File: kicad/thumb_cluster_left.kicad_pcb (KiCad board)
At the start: 2 copper layers, 41.2 x 46.6 mm, 18 parts, among them J1 Conn_01x07

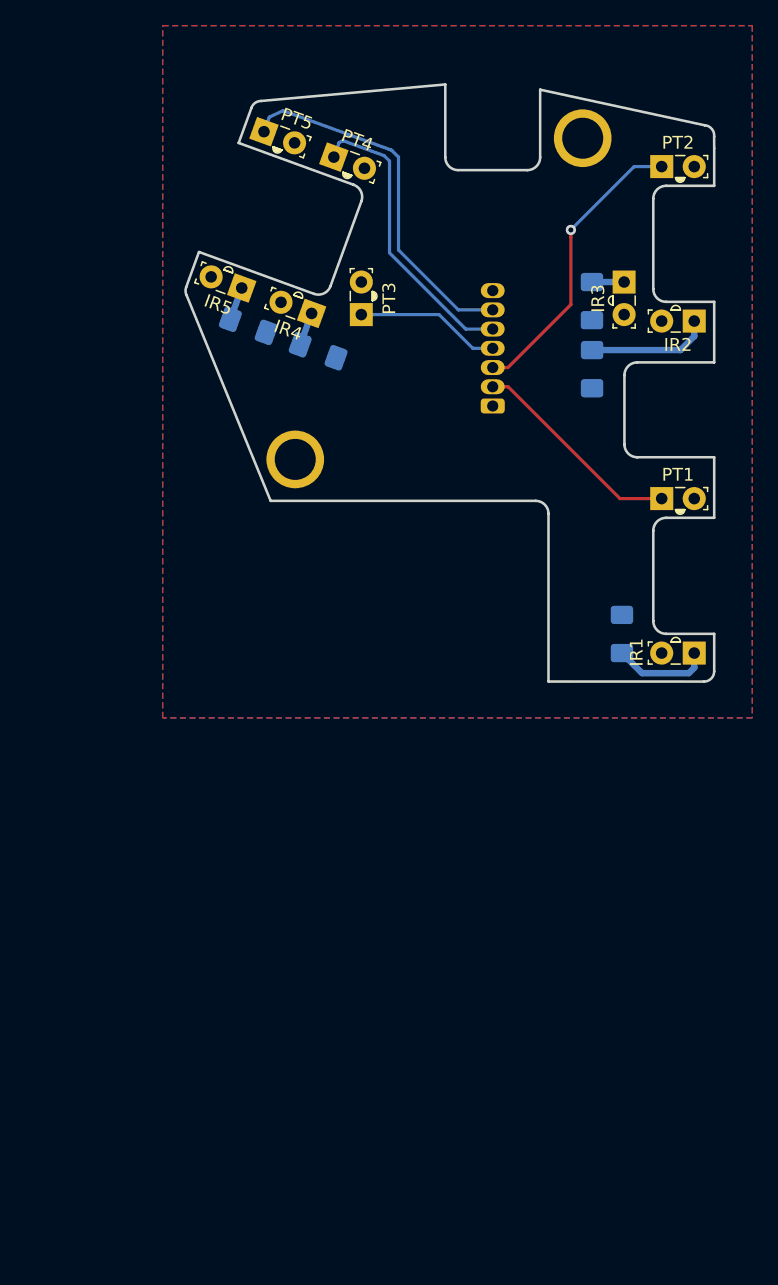
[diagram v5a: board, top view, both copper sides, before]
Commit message: Update thumb clusters to v2.5
Mostly just switching from 1206 to 0805 resistors, and some minor cleanup
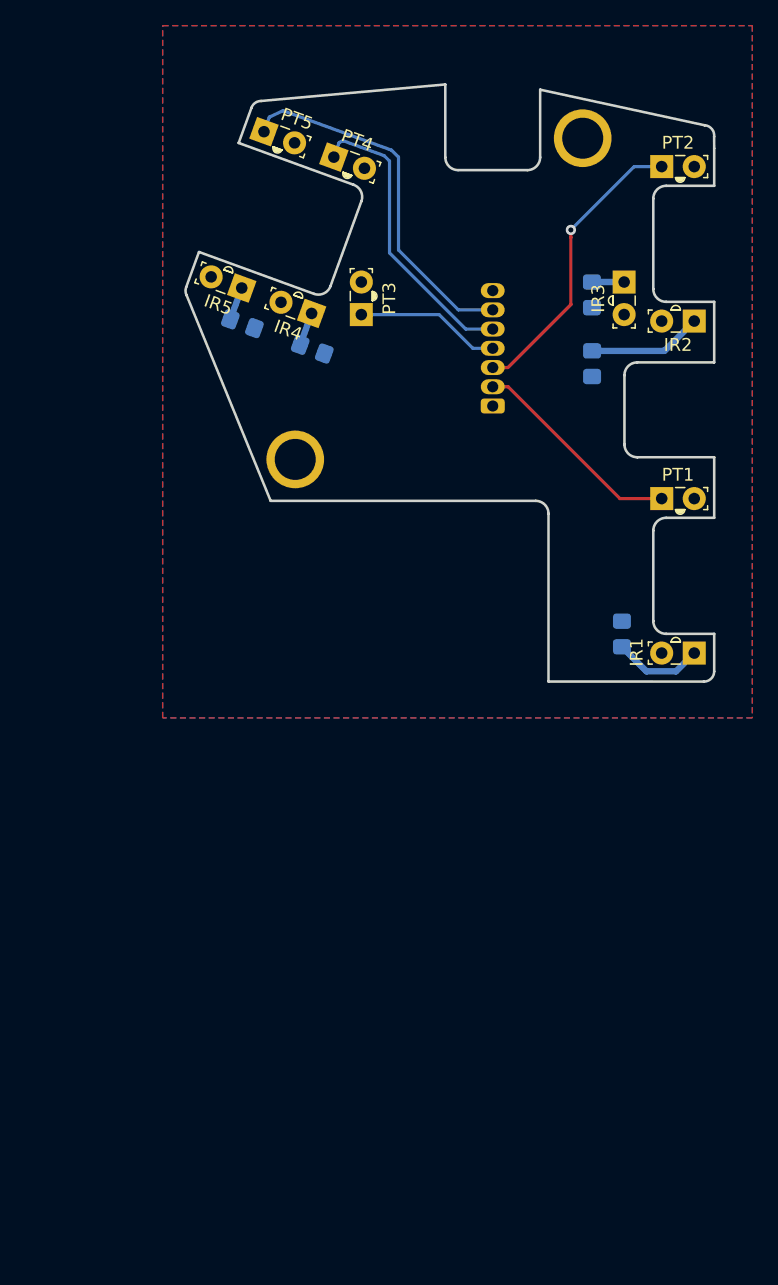
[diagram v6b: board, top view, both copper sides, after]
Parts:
- R1, R2, R3, R4, R5: footprint Resistor_SMD:R_1206_3216Metric_Pad1.42x1.75mm_HandSolder -> Resistor_SMD:R_0805_2012Metric_Pad1.20x1.40mm_HandSolder
- moved R4 0.49 mm to (143.2, 82.8)
- moved R3 0.49 mm to (165.0, 78.5)
- moved R5 0.49 mm to (137.7, 80.8)
- moved R2 0.43 mm to (165.0, 83.9)
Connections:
- net +5V renamed +3.3V
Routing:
- net Net-(IR2-K): track 9.60 -> 8.93 mm
- net Net-(IR1-K): track 7.61 -> 7.02 mm
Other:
- net class Default removed
- net class Power removed
- board text added: "lalboard.com left thumb cluster v2.5"
- board text removed: "Max internal corner radius: 1.0mm (for all internal corners)"
- board text removed: "lalboard.com left thumb cluster v0.2"

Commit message: Delete old lalboard.lib
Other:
- board text added: "lalboard.com left thumb cluster v2.5.0"
- board text removed: "lalboard.com left thumb cluster v2.5"
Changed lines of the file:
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@@
   (gr_line (start 174.524999 91.198958) (end 168.525 91.198959)
     (stroke (width 0.2) (type solid)) (layer "Edge.Cuts"))
-  (gr_text "lalboard.com\nleft thumb cluster\nv2.5" (at 154.978349 72.71453) (layer "B.SilkS")
+  (gr_text "lalboard.com\nleft thumb cluster\nv2.5.0" (at 154.978349 72.71453) (layer "B.SilkS")
     (effects (font (size 1 1) (thickness 0.15)) (justify mirror))
   )

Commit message: Add production files for the PCBs
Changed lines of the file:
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@@
     (grid_origin 150 100)
     (pcbplotparams
-      (layerselection 0x00210fc_ffffffff)
+      (layerselection 0x00010fc_ffffffff)
       (plot_on_all_layers_selection 0x0000000_00000000)
       (disableapertmacros false)
-      (usegerberextensions false)
-      (usegerberattributes true)
-      (usegerberadvancedattributes true)
-      (creategerberjobfile true)
+      (usegerberextensions true)
+      (usegerberattributes false)
+      (usegerberadvancedattributes false)
+      (creategerberjobfile false)
       (dashed_line_dash_ratio 12.000000)
       (dashed_line_gap_ratio 3.000000)
@@
       (psa4output false)
       (plotreference true)
-      (plotvalue true)
+      (plotvalue false)
       (plotinvisibletext false)
       (sketchpadsonfab false)
-      (subtractmaskfromsilk false)
+      (subtractmaskfromsilk true)
       (outputformat 1)
       (mirror false)
       (drillshape 0)
       (scaleselection 1)
-      (outputdirectory "/tmp/pcb")
+      (outputdirectory "/home/jesusfreke/projects/lalboard/kicad/production_files/thumb_left/")
     )
   )
@@
     (fp_line (start 10.5 1.3) (end -1.5 1.3)
       (stroke (width 0.1) (type solid)) (layer "B.Fab"))
-    (pad "1" thru_hole roundrect (at 0 0 90) (size 1.17 1.87) (drill 0.87) (layers "*.Cu" "*.Mask") (roundrect_rratio 0.213675)
+    (pad "1" thru_hole roundrect (at 0 0 90) (size 1.17 1.87) (drill 0.87) (layers "*.Cu" "*.Mask") (roundrect_rratio 0.2136752137)
       (net 8 "+3.3V") (pinfunction "Pin_1") (pintype "passive"))
     (pad "2" thru_hole oval (at 1.5 0 90) (size 1.17 1.87) (drill 0.87) (layers "*.Cu" "*.Mask")
@@
     (fp_line (start 1 0.625) (end 1 -0.625)
       (stroke (width 0.1) (type solid)) (layer "B.Fab"))
-    (pad "1" smd roundrect (at -1 0 90) (size 1.2 1.4) (layers "B.Cu" "B.Paste" "B.Mask") (roundrect_rratio 0.208333)
+    (pad "1" smd roundrect (at -1 0 90) (size 1.2 1.4) (layers "B.Cu" "B.Paste" "B.Mask") (roundrect_rratio 0.2083333333)
       (net 2 "GND") (pintype "passive"))
-    (pad "2" smd roundrect (at 1 0 90) (size 1.2 1.4) (layers "B.Cu" "B.Paste" "B.Mask") (roundrect_rratio 0.208333)
+    (pad "2" smd roundrect (at 1 0 90) (size 1.2 1.4) (layers "B.Cu" "B.Paste" "B.Mask") (roundrect_rratio 0.2083333333)
       (net 10 "Net-(IR3-K)") (pintype "passive"))
     (model "${KICAD6_3DMODEL_DIR}/Resistor_SMD.3dshapes/R_0805_2012Metric.wrl"
@@
     (fp_line (start 1 0.625) (end 1 -0.625)
       (stroke (width 0.1) (type solid)) (layer "B.Fab"))
-    (pad "1" smd roundrect (at -1 0 90) (size 1.2 1.4) (layers "B.Cu" "B.Paste" "B.Mask") (roundrect_rratio 0.208333)
+    (pad "1" smd roundrect (at -1 0 90) (size 1.2 1.4) (layers "B.Cu" "B.Paste" "B.Mask") (roundrect_rratio 0.2083333333)
       (net 2 "GND") (pintype "passive"))
-    (pad "2" smd roundrect (at 1 0 90) (size 1.2 1.4) (layers "B.Cu" "B.Paste" "B.Mask") (roundrect_rratio 0.208333)
+    (pad "2" smd roundrect (at 1 0 90) (size 1.2 1.4) (layers "B.Cu" "B.Paste" "B.Mask") (roundrect_rratio 0.2083333333)
       (net 9 "Net-(IR2-K)") (pintype "passive"))
     (model "${KICAD6_3DMODEL_DIR}/Resistor_SMD.3dshapes/R_0805_2012Metric.wrl"
@@
     (fp_line (start 1 0.625) (end 1 -0.625)
       (stroke (width 0.1) (type solid)) (layer "B.Fab"))
-    (pad "1" smd roundrect (at -1 0 160) (size 1.2 1.4) (layers "B.Cu" "B.Paste" "B.Mask") (roundrect_rratio 0.208333)
+    (pad "1" smd roundrect (at -1 0 160) (size 1.2 1.4) (layers "B.Cu" "B.Paste" "B.Mask") (roundrect_rratio 0.2083333333)
       (net 2 "GND") (pintype "passive"))
-    (pad "2" smd roundrect (at 1 0 160) (size 1.2 1.4) (layers "B.Cu" "B.Paste" "B.Mask") (roundrect_rratio 0.208333)
+    (pad "2" smd roundrect (at 1 0 160) (size 1.2 1.4) (layers "B.Cu" "B.Paste" "B.Mask") (roundrect_rratio 0.2083333333)
       (net 12 "Net-(IR5-K)") (pintype "passive"))
     (model "${KICAD6_3DMODEL_DIR}/Resistor_SMD.3dshapes/R_0805_2012Metric.wrl"
@@
     (fp_line (start 1 0.625) (end 1 -0.625)
       (stroke (width 0.1) (type solid)) (layer "B.Fab"))
-    (pad "1" smd roundrect (at -1 0 270) (size 1.2 1.4) (layers "B.Cu" "B.Paste" "B.Mask") (roundrect_rratio 0.208333)
+    (pad "1" smd roundrect (at -1 0 270) (size 1.2 1.4) (layers "B.Cu" "B.Paste" "B.Mask") (roundrect_rratio 0.2083333333)
       (net 2 "GND") (pintype "passive"))
-    (pad "2" smd roundrect (at 1 0 270) (size 1.2 1.4) (layers "B.Cu" "B.Paste" "B.Mask") (roundrect_rratio 0.208333)
+    (pad "2" smd roundrect (at 1 0 270) (size 1.2 1.4) (layers "B.Cu" "B.Paste" "B.Mask") (roundrect_rratio 0.2083333333)
       (net 1 "Net-(IR1-K)") (pintype "passive"))
     (model "${KICAD6_3DMODEL_DIR}/Resistor_SMD.3dshapes/R_0805_2012Metric.wrl"
@@
     (fp_line (start 1 0.625) (end 1 -0.625)
       (stroke (width 0.1) (type solid)) (layer "B.Fab"))
-    (pad "1" smd roundrect (at -1 0 160) (size 1.2 1.4) (layers "B.Cu" "B.Paste" "B.Mask") (roundrect_rratio 0.208333)
+    (pad "1" smd roundrect (at -1 0 160) (size 1.2 1.4) (layers "B.Cu" "B.Paste" "B.Mask") (roundrect_rratio 0.2083333333)
       (net 2 "GND") (pintype "passive"))
-    (pad "2" smd roundrect (at 1 0 160) (size 1.2 1.4) (layers "B.Cu" "B.Paste" "B.Mask") (roundrect_rratio 0.208333)
+    (pad "2" smd roundrect (at 1 0 160) (size 1.2 1.4) (layers "B.Cu" "B.Paste" "B.Mask") (roundrect_rratio 0.2083333333)
       (net 11 "Net-(IR4-K)") (pintype "passive"))
     (model "${KICAD6_3DMODEL_DIR}/Resistor_SMD.3dshapes/R_0805_2012Metric.wrl"
